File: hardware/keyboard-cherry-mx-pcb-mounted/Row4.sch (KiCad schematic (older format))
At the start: 28 parts, among them SW46 LShift, SW47 ,, SW48 z, SW49 ., SW50 x, SW51 /, SW52 c, SW53 RShift, SW54 v, SW55 Up Arrow, SW56 b, SW57 End, SW58 n, SW59 m

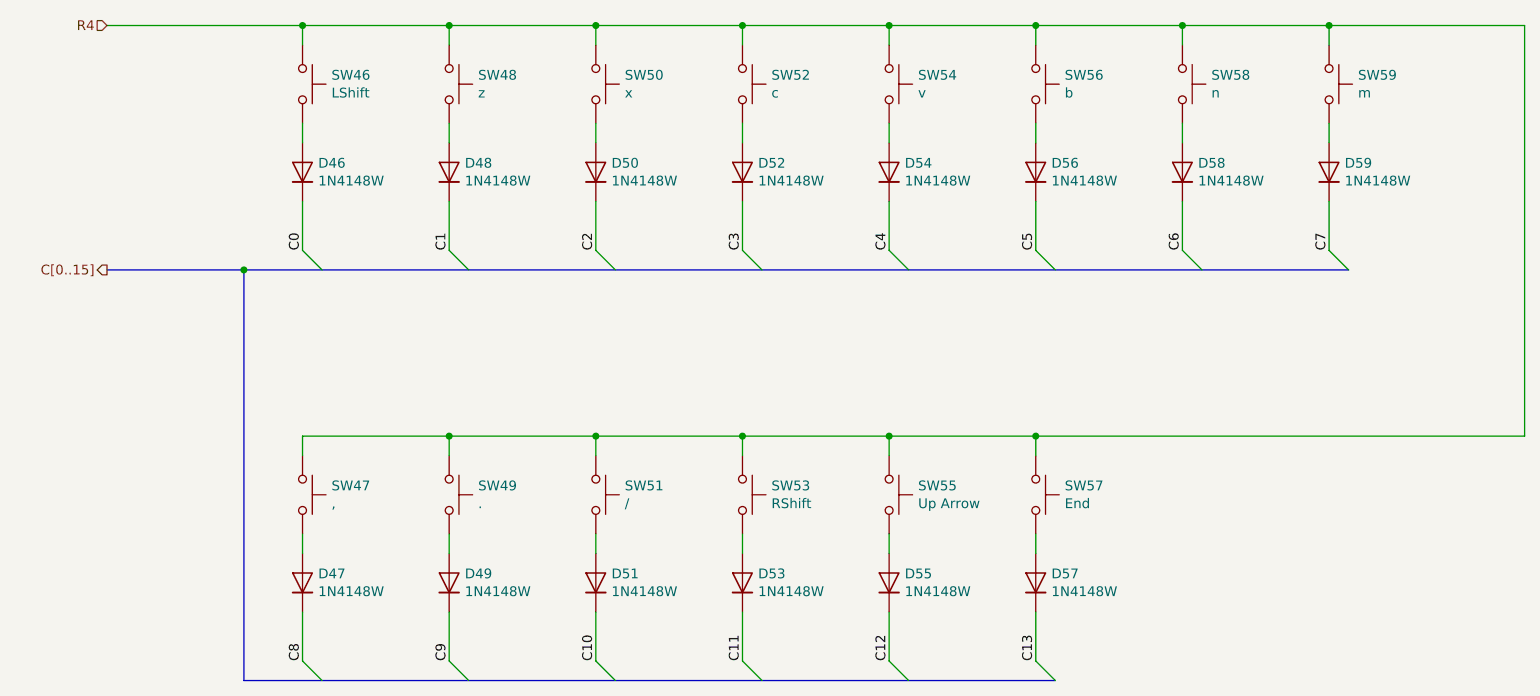
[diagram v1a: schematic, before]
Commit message: Adds completed sensor and power connections. Still need to add USB footprint then sch are done for version 1.0
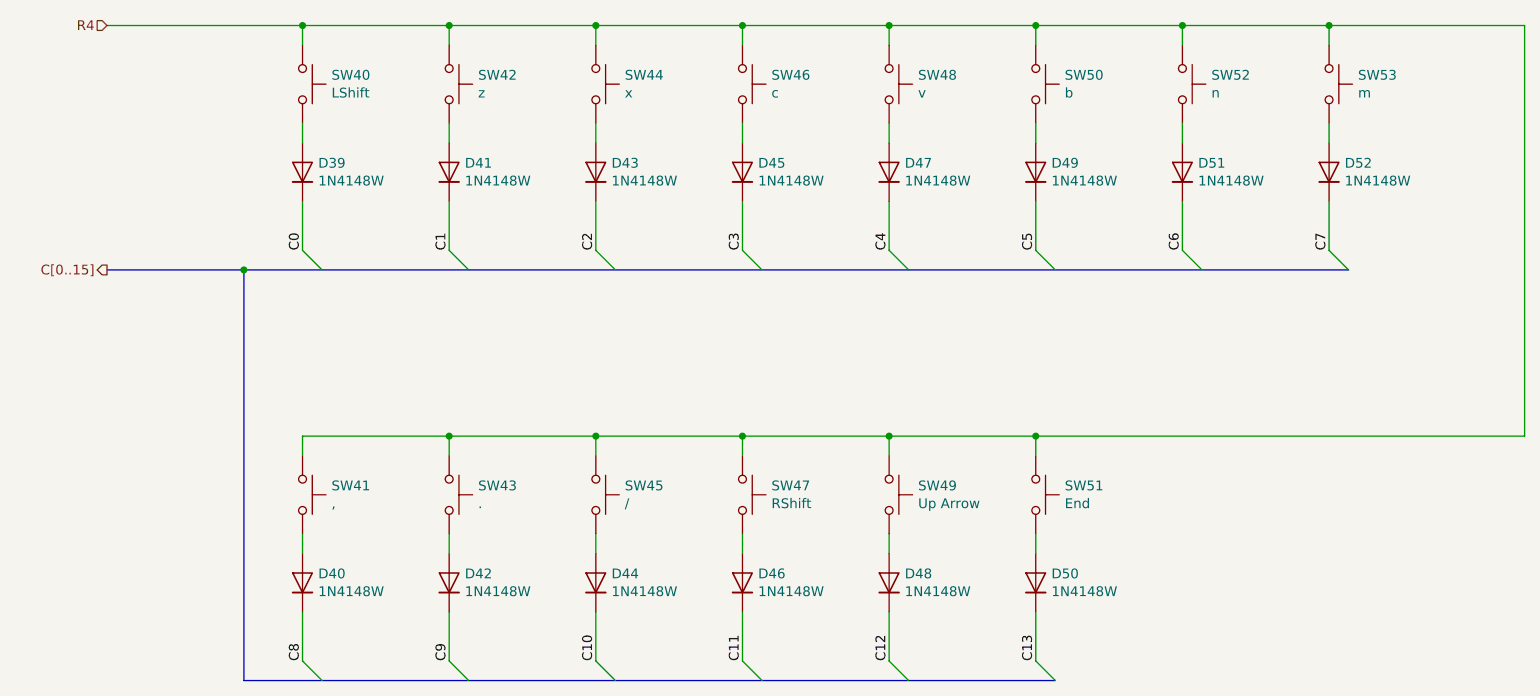
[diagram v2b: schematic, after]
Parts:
- renumbered D46 to D39, D47 to D40, D48 to D41, D49 to D42, D50 to D43, D51 to D44, D52 to D45, D53 to D46, D54 to D47, D55 to D48, D56 to D49, D57 to D50, D58 to D51, D59 to D52, SW46 to SW40, SW47 to SW41, SW48 to SW42, SW49 to SW43, SW50 to SW44, SW51 to SW45, SW52 to SW46, SW53 to SW47, SW54 to SW48, SW55 to SW49, SW56 to SW50, SW57 to SW51, SW58 to SW52, SW59 to SW53

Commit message: Aligns the keys so the column connections are more consistent. e.g. right most keys will have same column connection.
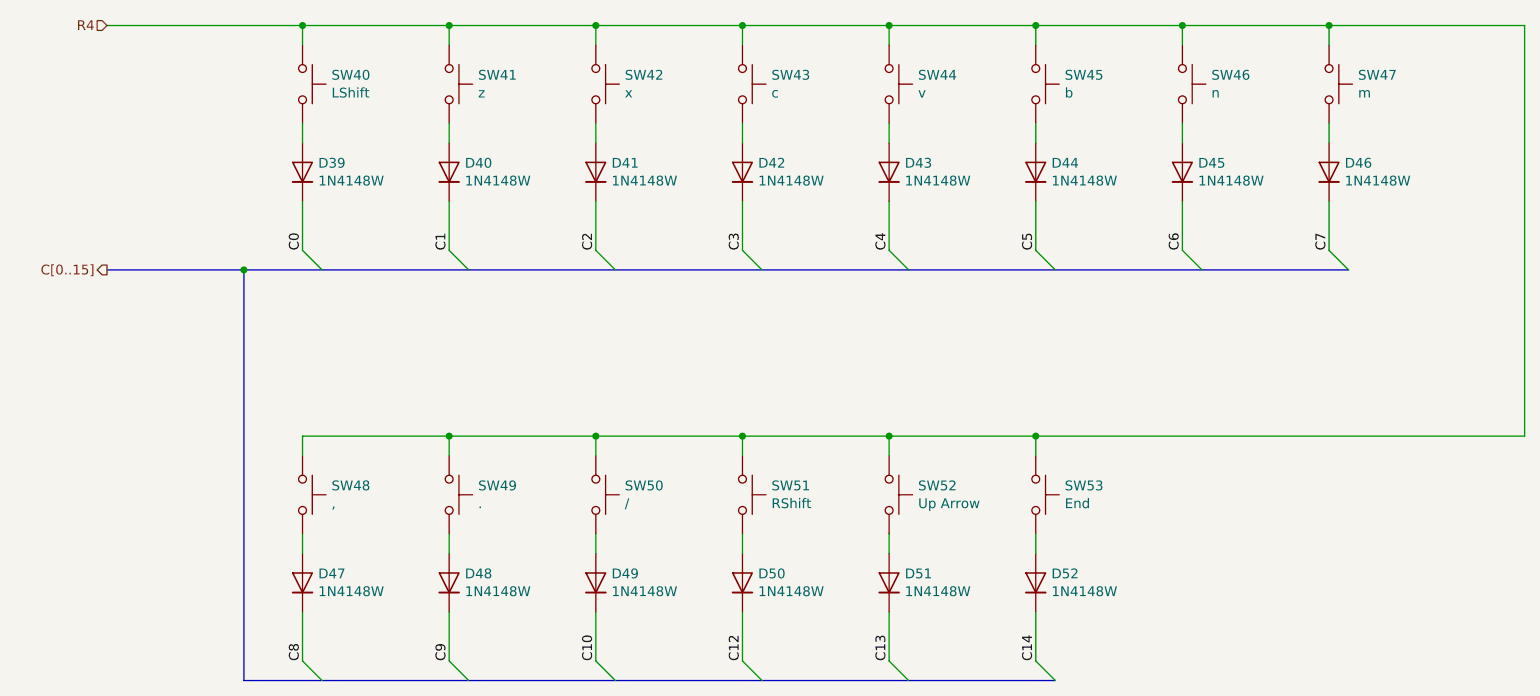
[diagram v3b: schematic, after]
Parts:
- renumbered D41 to D40, D43 to D41, D45 to D42, D47 to D43, D49 to D44, D51 to D45, D52 to D46, D40 to D47, D42 to D48, D44 to D49, D46 to D50, D48 to D51, D50 to D52, SW42 to SW41, SW44 to SW42, SW46 to SW43, SW48 to SW44, SW50 to SW45, SW52 to SW46, SW53 to SW47, SW41 to SW48, SW43 to SW49, SW45 to SW50, SW47 to SW51, SW49 to SW52, SW51 to SW53
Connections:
- net C11 is gone; now on net C12: D50.1 (K)
- net C12: no longer D51.1 (K)
- net C13: now also D51.1 (K); no longer D52.1 (K)
- new net C14: D52.1 (K)

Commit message: Adds labels for each key and creates gerber files.
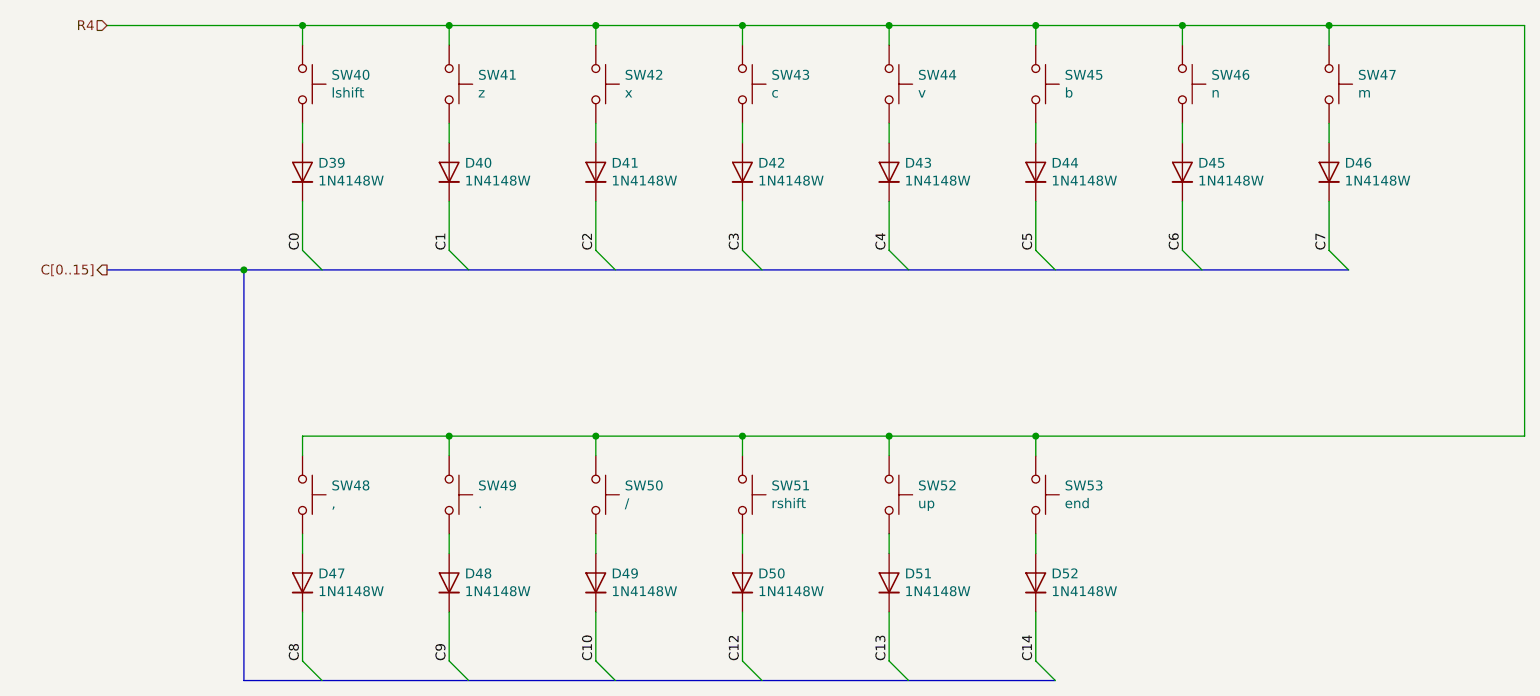
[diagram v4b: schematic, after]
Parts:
- SW40: value LShift -> lshift
- SW51: value RShift -> rshift
- SW52: value Up Arrow -> up
- SW53: value End -> end
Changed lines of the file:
@@
 AR Path="/5E697948/5E78F98F/5E79006F" Ref="SW?"  Part="1"
 F 0 "SW40" V 3104 2548 50  0000 L CNN
-F 1 "LShift" V 3195 2548 50  0000 L CNN
+F 1 "lshift" V 3195 2548 50  0000 L CNN
 F 2 "Button_Switch_Keyboard:SW_Cherry_MX_2.25u_PCB" H 3150 2600 50  0001 C CNN
 F 3 "~" H 3150 2600 50  0001 C CNN
@@
 AR Path="/5E697948/5E78F98F/5E77F01C" Ref="SW?"  Part="1"
 F 0 "SW51" V 5354 4648 50  0000 L CNN
-F 1 "RShift" V 5445 4648 50  0000 L CNN
+F 1 "rshift" V 5445 4648 50  0000 L CNN
 F 2 "Button_Switch_Keyboard:SW_Cherry_MX_1.75u_PCB" H 5400 4700 50  0001 C CNN
 F 3 "~" H 5400 4700 50  0001 C CNN
@@
 AR Path="/5E697948/5E78F98F/5E790087" Ref="SW?"  Part="1"
 F 0 "SW52" V 6104 4648 50  0000 L CNN
-F 1 "Up Arrow" V 6195 4648 50  0000 L CNN
+F 1 "up" V 6195 4648 50  0000 L CNN
 F 2 "Button_Switch_Keyboard:SW_Cherry_MX_1.00u_PCB" H 6150 4700 50  0001 C CNN
 F 3 "~" H 6150 4700 50  0001 C CNN
@@
 AR Path="/5E697948/5E78F98F/5E790089" Ref="SW?"  Part="1"
 F 0 "SW53" V 6854 4648 50  0000 L CNN
-F 1 "End" V 6945 4648 50  0000 L CNN
+F 1 "end" V 6945 4648 50  0000 L CNN
 F 2 "Button_Switch_Keyboard:SW_Cherry_MX_1.00u_PCB" H 6900 4700 50  0001 C CNN
 F 3 "~" H 6900 4700 50  0001 C CNN
